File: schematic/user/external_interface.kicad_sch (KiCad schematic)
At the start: 36 parts, among them J10 Radio Audio, J2 Radio_Jack, J3 User_Jack, J5 PTT Breakout, J9 User Audio, Q3 MBT3904DW1T1, Q4 MBT3904DW1T1, Q5 MBT3904DW1T1, Q6 MBT3904DW1T1, SW3 PTT_Button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

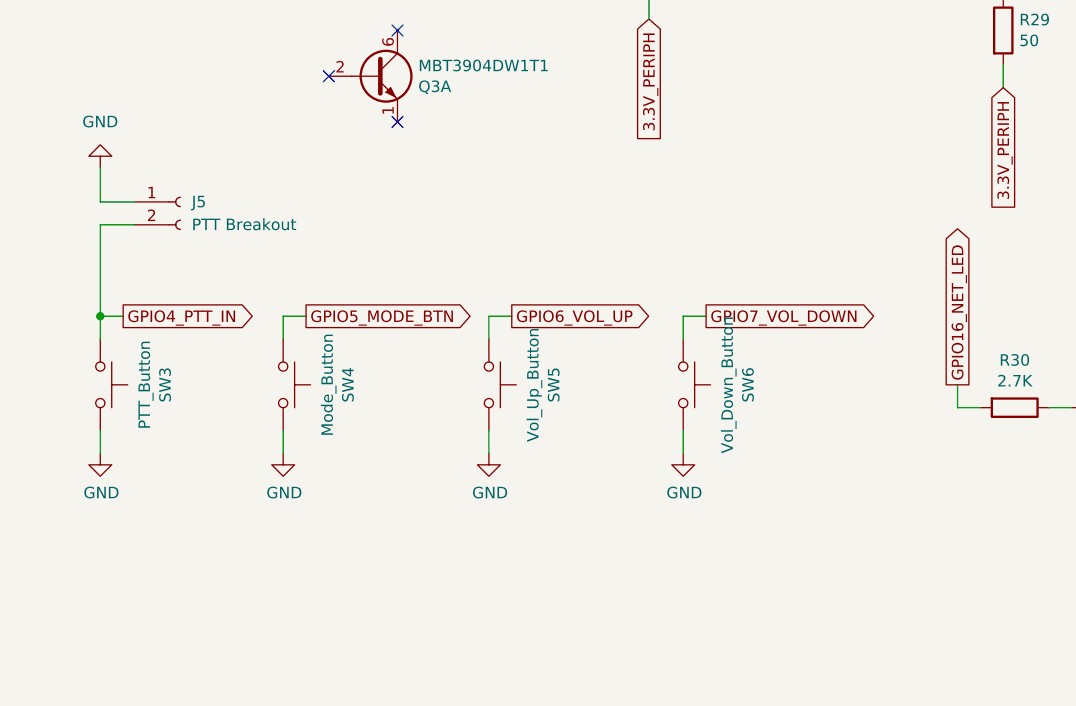
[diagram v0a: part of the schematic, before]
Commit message: v0.7 board: add TVS protection for buttons.
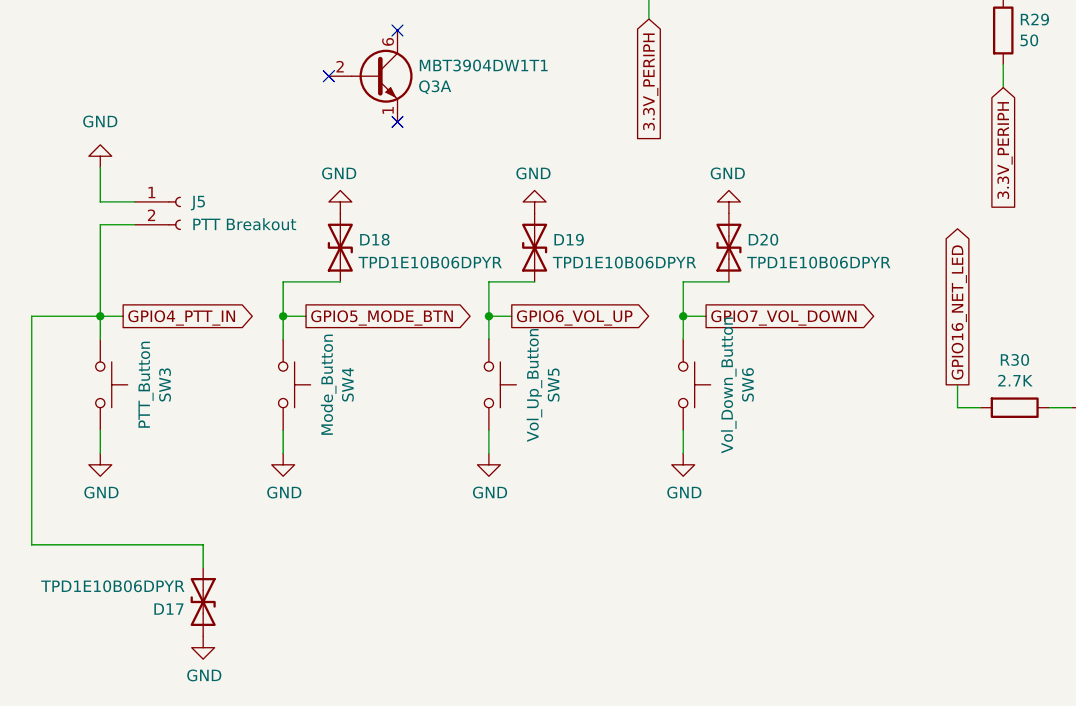
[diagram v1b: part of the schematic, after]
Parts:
- added D17, D18, D19, D20: TPD1E10B06DPYR, ezDV_production:DIO_TPD1E05U06DPYR, symbol Device:D_TVS
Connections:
- net GND: now also D17.2 (A2), D18.2 (A2), D19.2 (A2), D20.2 (A2)
- net GPIO4_PTT_IN: now also D17.1 (A1)
- net GPIO5_MODE_BTN: now also D18.1 (A1)
- net GPIO6_VOL_UP: now also D19.1 (A1)
- net GPIO7_VOL_DOWN: now also D20.1 (A1)
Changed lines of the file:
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@@
   (junction (at 120.65 33.02) (diameter 0) (color 0 0 0 0)
   )
+  (junction (at 66.04 142.24) (diameter 0) (color 0 0 0 0)
+  )
   (junction (at 104.14 38.1) (diameter 0) (color 0 0 0 0)
   )
@@
   (junction (at 116.84 35.56) (diameter 0) (color 0 0 0 0)
   )
+  (junction (at 43.18 142.24) (diameter 0) (color 0 0 0 0)
+  )
   (junction (at 55.88 31.75) (diameter 0) (color 0 0 0 0)
   )
@@
   )
   (junction (at 114.3 30.48) (diameter 0) (color 0 0 0 0)
+  )
+  (junction (at 87.63 142.24) (diameter 0) (color 0 0 0 0)
   )
   (no_connect (at 55.88 120.65))
@@
     (stroke (width 0) (type default) (color 0 0 0 0))
   )
+  (wire (pts (xy 15.24 167.64) (xy 34.29 167.64))
+    (stroke (width 0) (type default) (color 0 0 0 0))
+  )
   (wire (pts (xy 162.56 91.44) (xy 162.56 88.9))
     (stroke (width 0) (type default) (color 0 0 0 0))
@@
     (stroke (width 0) (type default) (color 0 0 0 0))
   )
+  (wire (pts (xy 22.86 142.24) (xy 15.24 142.24))
+    (stroke (width 0) (type default) (color 0 0 0 0))
+  )
   (wire (pts (xy 133.35 88.9) (xy 130.81 88.9))
     (stroke (width 0) (type default) (color 0 0 0 0))
@@
     (stroke (width 0) (type default) (color 0 0 0 0))
   )
+  (wire (pts (xy 15.24 142.24) (xy 15.24 167.64))
+    (stroke (width 0) (type default) (color 0 0 0 0))
+  )
   (wire (pts (xy 133.35 78.74) (xy 133.35 76.2))
     (stroke (width 0) (type default) (color 0 0 0 0))
@@
     (stroke (width 0) (type default) (color 0 0 0 0))
   )
+  (wire (pts (xy 87.63 142.24) (xy 87.63 138.43))
+    (stroke (width 0) (type default) (color 0 0 0 0))
+  )
   (wire (pts (xy 101.6 30.48) (xy 114.3 30.48))
     (stroke (width 0) (type default) (color 0 0 0 0))
@@
     (stroke (width 0) (type default) (color 0 0 0 0))
   )
+  (wire (pts (xy 66.04 138.43) (xy 71.12 138.43))
+    (stroke (width 0) (type default) (color 0 0 0 0))
+  )
   (wire (pts (xy 83.82 76.2) (xy 83.82 73.66))
     (stroke (width 0) (type default) (color 0 0 0 0))
@@
     (stroke (width 0) (type default) (color 0 0 0 0))
   )
+  (wire (pts (xy 43.18 138.43) (xy 49.53 138.43))
+    (stroke (width 0) (type default) (color 0 0 0 0))
+  )
   (wire (pts (xy 157.48 29.21) (xy 160.02 29.21))
     (stroke (width 0) (type default) (color 0 0 0 0))
@@
     (stroke (width 0) (type default) (color 0 0 0 0))
   )
+  (wire (pts (xy 87.63 138.43) (xy 92.71 138.43))
+    (stroke (width 0) (type default) (color 0 0 0 0))
+  )
   (wire (pts (xy 118.11 152.4) (xy 118.11 149.86))
     (stroke (width 0) (type default) (color 0 0 0 0))
@@
     (stroke (width 0) (type default) (color 0 0 0 0))
   )
+  (wire (pts (xy 43.18 142.24) (xy 43.18 138.43))
+    (stroke (width 0) (type default) (color 0 0 0 0))
+  )
   (wire (pts (xy 101.6 27.94) (xy 104.14 27.94))
     (stroke (width 0) (type default) (color 0 0 0 0))
@@
     (stroke (width 0) (type default) (color 0 0 0 0))
   )
+  (wire (pts (xy 66.04 142.24) (xy 66.04 138.43))
+    (stroke (width 0) (type default) (color 0 0 0 0))
+  )
   (wire (pts (xy 200.66 27.94) (xy 198.12 27.94))
     (stroke (width 0) (type default) (color 0 0 0 0))
@@
   )
   (wire (pts (xy 162.56 66.04) (xy 162.56 68.58))
+    (stroke (width 0) (type default) (color 0 0 0 0))
+  )
+  (wire (pts (xy 34.29 167.64) (xy 34.29 170.18))
     (stroke (width 0) (type default) (color 0 0 0 0))
   )
@@
     (pin "5")
   )
+  (symbol (lib_id "power:GND") (at 49.53 130.81 180) (unit 1)
+    (in_bom yes) (on_board yes)
+    (property "Reference" "#PWR059" (id 0) (at 49.53 124.46 0)
+      (effects (font (size 1.27 1.27)) hide)
+    )
+    (property "Value" "GND" (id 1) (at 49.403 126.4158 0))
+    (property "Footprint" "" (id 2) (at 49.53 130.81 0)
+      (effects (font (size 1.27 1.27)) hide)
+    )
+    (property "Datasheet" "" (id 3) (at 49.53 130.81 0)
+      (effects (font (size 1.27 1.27)) hide)
+    )
+    (pin "1")
+  )
+  (symbol (lib_id "Device:D_TVS") (at 92.71 134.62 90) (unit 1)
+    (in_bom yes) (on_board yes) (fields_autoplaced)
+    (property "Reference" "D20" (id 0) (at 94.742 133.7853 90)
+      (effects (font (size 1.27 1.27)) (justify right))
+    )
+    (property "Value" "TPD1E10B06DPYR" (id 1) (at 94.742 136.3222 90)
+      (effects (font (size 1.27 1.27)) (justify right))
+    )
+    (property "Footprint" "ezDV_production:DIO_TPD1E05U06DPYR" (id 2) (at 92.71 134.62 0)
+      (effects (font (size 1.27 1.27)) hide)
+    )
+    (property "Datasheet" "https://www.ti.com/lit/ds/symlink/tpd1e10b06.pdf?ts=1673062853444" (id 3) (at 92.71 134.62 0)
+      (effects (font (size 1.27 1.27)) hide)
+    )
+    (property "LCSC" "C48260" (id 4) (at 92.71 134.62 90)
+      (effects (font (size 1.27 1.27)) hide)
+    )
+    (pin "1")
+    (pin "2")
+  )
+  (symbol (lib_id "power:GND") (at 71.12 130.81 180) (unit 1)
+    (in_bom yes) (on_board yes)
+    (property "Reference" "#PWR060" (id 0) (at 71.12 124.46 0)
+      (effects (font (size 1.27 1.27)) hide)
+    )
+    (property "Value" "GND" (id 1) (at 70.993 126.4158 0))
+    (property "Footprint" "" (id 2) (at 71.12 130.81 0)
+      (effects (font (size 1.27 1.27)) hide)
+    )
+    (property "Datasheet" "" (id 3) (at 71.12 130.81 0)
+      (effects (font (size 1.27 1.27)) hide)
+    )
+    (pin "1")
+  )
   (symbol (lib_id "power:GND") (at 261.62 106.68 0) (unit 1)
     (in_bom yes) (on_board yes)
@@
     (pin "2")
   )
+  (symbol (lib_id "power:GND") (at 92.71 130.81 180) (unit 1)
+    (in_bom yes) (on_board yes)
+    (property "Reference" "#PWR061" (id 0) (at 92.71 124.46 0)
+      (effects (font (size 1.27 1.27)) hide)
+    )
+    (property "Value" "GND" (id 1) (at 92.583 126.4158 0))
+    (property "Footprint" "" (id 2) (at 92.71 130.81 0)
+      (effects (font (size 1.27 1.27)) hide)
+    )
+    (property "Datasheet" "" (id 3) (at 92.71 130.81 0)
+      (effects (font (size 1.27 1.27)) hide)
+    )
+    (pin "1")
+  )
   (symbol (lib_id "Device:LED") (at 123.19 100.33 270) (unit 1)
     (in_bom yes) (on_board yes)
@@
     )
     (pin "1")
+  )
+  (symbol (lib_id "Device:D_TVS") (at 71.12 134.62 90) (unit 1)
+    (in_bom yes) (on_board yes) (fields_autoplaced)
+    (property "Reference" "D19" (id 0) (at 73.152 133.7853 90)
+      (effects (font (size 1.27 1.27)) (justify right))
+    )
+    (property "Value" "TPD1E10B06DPYR" (id 1) (at 73.152 136.3222 90)
+      (effects (font (size 1.27 1.27)) (justify right))
+    )
+    (property "Footprint" "ezDV_production:DIO_TPD1E05U06DPYR" (id 2) (at 71.12 134.62 0)
+      (effects (font (size 1.27 1.27)) hide)
+    )
+    (property "Datasheet" "https://www.ti.com/lit/ds/symlink/tpd1e10b06.pdf?ts=1673062853444" (id 3) (at 71.12 134.62 0)
+      (effects (font (size 1.27 1.27)) hide)
+    )
+    (property "LCSC" "C48260" (id 4) (at 71.12 134.62 90)
+      (effects (font (size 1.27 1.27)) hide)
+    )
+    (pin "1")
+    (pin "2")
   )
   (symbol (lib_id "power:GND") (at 138.43 160.02 0) (unit 1)
@@
     (pin "2")
   )
+  (symbol (lib_id "Device:D_TVS") (at 34.29 173.99 270) (unit 1)
+    (in_bom yes) (on_board yes)
+    (property "Reference" "D17" (id 0) (at 32.258 174.8247 90)
+      (effects (font (size 1.27 1.27)) (justify right))
+    )
+    (property "Value" "TPD1E10B06DPYR" (id 1) (at 32.258 172.2878 90)
+      (effects (font (size 1.27 1.27)) (justify right))
+    )
+    (property "Footprint" "ezDV_production:DIO_TPD1E05U06DPYR" (id 2) (at 34.29 173.99 0)
+      (effects (font (size 1.27 1.27)) hide)
+    )
+    (property "Datasheet" "https://www.ti.com/lit/ds/symlink/tpd1e10b06.pdf?ts=1673062853444" (id 3) (at 34.29 173.99 0)
+      (effects (font (size 1.27 1.27)) hide)
+    )
+    (property "LCSC" "C48260" (id 4) (at 34.29 173.99 90)
+      (effects (font (size 1.27 1.27)) hide)
+    )
+    (pin "1")
+    (pin "2")
+  )
   (symbol (lib_id "Switch:SW_Push") (at 66.04 149.86 270) (unit 1)
     (in_bom yes) (on_board yes)
@@
     (pin "3")
     (pin "4")
+  )
+  (symbol (lib_id "Device:D_TVS") (at 49.53 134.62 90) (unit 1)
+    (in_bom yes) (on_board yes)
+    (property "Reference" "D18" (id 0) (at 51.562 133.7853 90)
+      (effects (font (size 1.27 1.27)) (justify right))
+    )
+    (property "Value" "TPD1E10B06DPYR" (id 1) (at 51.562 136.3222 90)
+      (effects (font (size 1.27 1.27)) (justify right))
+    )
+    (property "Footprint" "ezDV_production:DIO_TPD1E05U06DPYR" (id 2) (at 49.53 134.62 0)
+      (effects (font (size 1.27 1.27)) hide)
+    )
+    (property "Datasheet" "https://www.ti.com/lit/ds/symlink/tpd1e10b06.pdf?ts=1673062853444" (id 3) (at 49.53 134.62 0)
+      (effects (font (size 1.27 1.27)) hide)
+    )
+    (property "LCSC" "C48260" (id 4) (at 49.53 134.62 90)
+      (effects (font (size 1.27 1.27)) hide)
+    )
+    (pin "1")
+    (pin "2")
   )
   (symbol (lib_id "power:GND") (at 104.14 27.94 90) (unit 1)
@@
     (pin "5")
   )
+  (symbol (lib_id "power:GND") (at 34.29 177.8 0) (unit 1)
+    (in_bom yes) (on_board yes)
+    (property "Reference" "#PWR058" (id 0) (at 34.29 184.15 0)
+      (effects (font (size 1.27 1.27)) hide)
+    )
+    (property "Value" "GND" (id 1) (at 34.417 182.1942 0))
+    (property "Footprint" "" (id 2) (at 34.29 177.8 0)
+      (effects (font (size 1.27 1.27)) hide)
+    )
+    (property "Datasheet" "" (id 3) (at 34.29 177.8 0)
+      (effects (font (size 1.27 1.27)) hide)
+    )
+    (pin "1")
+  )
   (symbol (lib_id "Device:LED") (at 162.56 85.09 270) (unit 1)

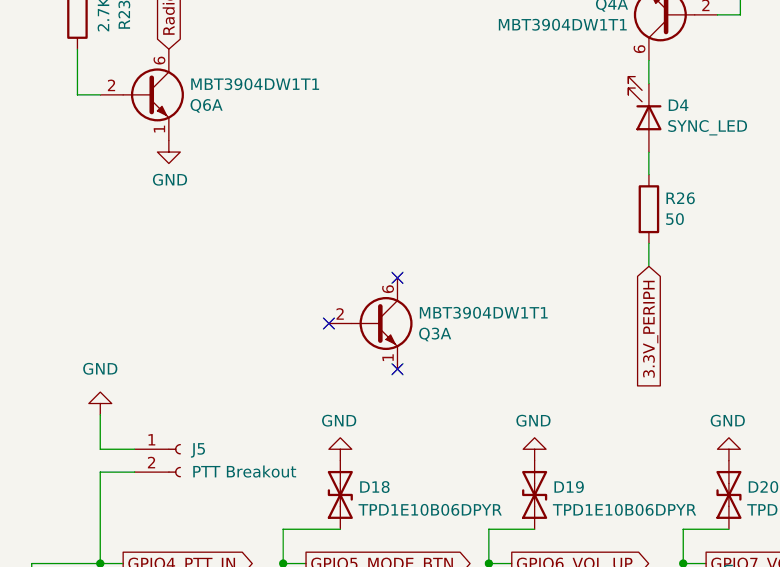
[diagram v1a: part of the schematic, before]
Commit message: v0.7 board: add WUSB3801 and reduce TP4056 max current if USB port doesn't support >=1.5A current.
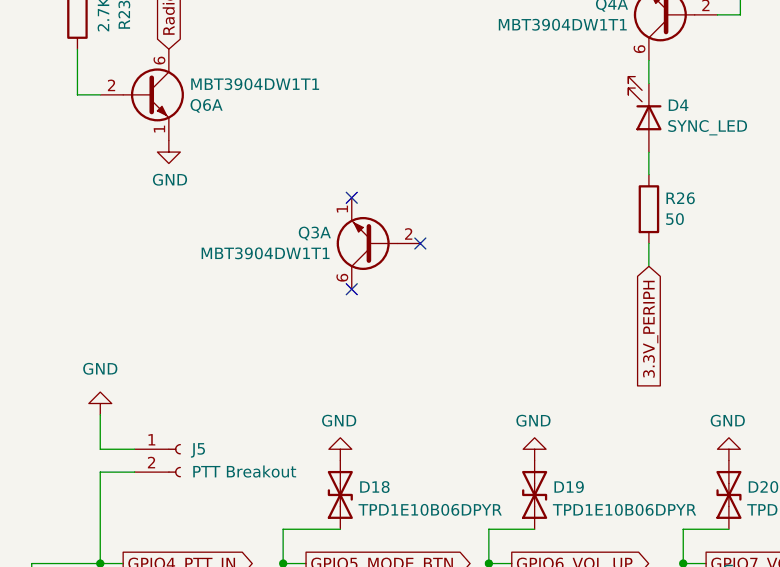
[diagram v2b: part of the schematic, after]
